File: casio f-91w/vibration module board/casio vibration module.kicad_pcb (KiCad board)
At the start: 2 copper layers, 27 x 25.3 mm, 5 parts

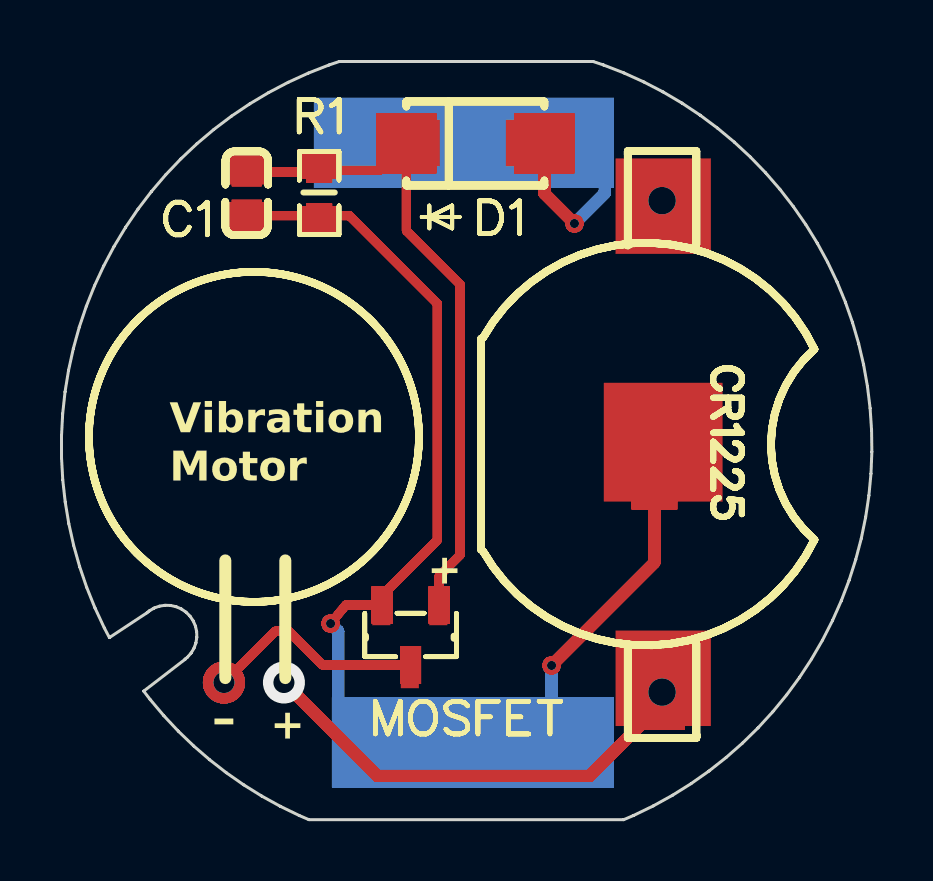
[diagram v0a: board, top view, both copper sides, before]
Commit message: Update vibration module to use 100k resistor
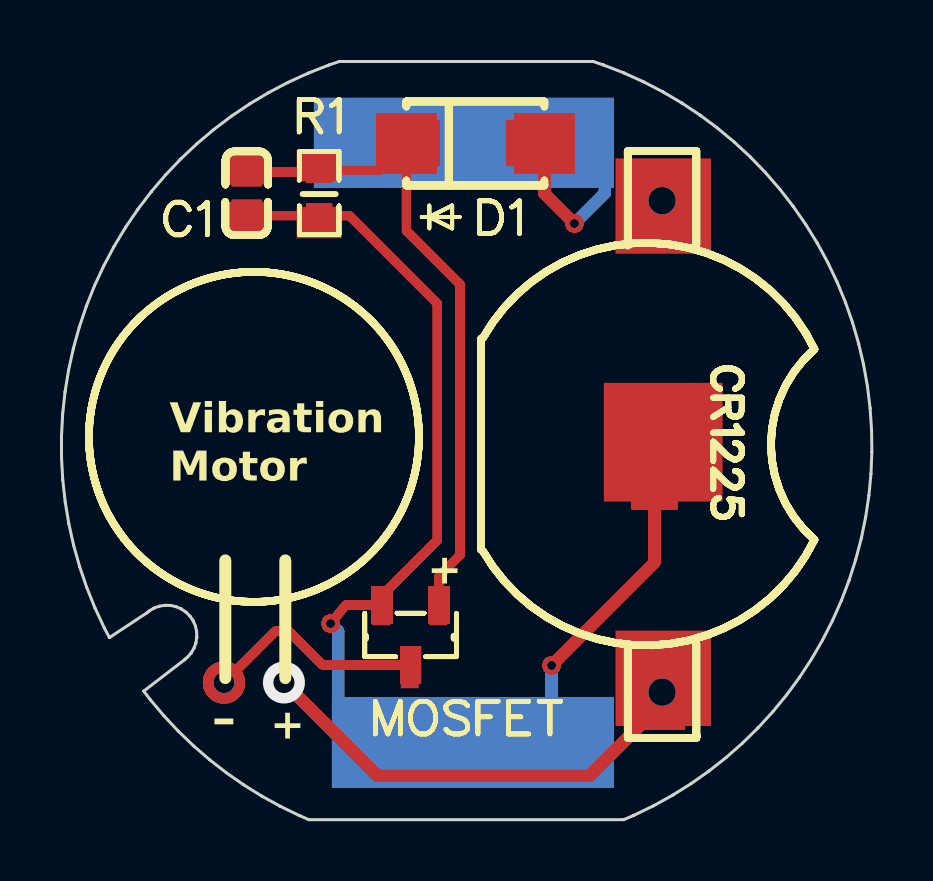
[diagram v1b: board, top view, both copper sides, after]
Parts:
- removed the R** at (135.8, 134.3)
- added R**: RESC2013X65N, footprints:WCR0805LF1003FPLT, F.Cu at (135.8, 134.3)
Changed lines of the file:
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@@
+		)
+	)
+	(footprint "footprints:WCR0805LF1003FPLT"
+		(layer "F.Cu")
+		(at 135.828 134.3276 90)
+		(descr "WCR0805-ren1")
+		(tags "Resistor")
+		(property "Reference" "R**"
+			(at -3.3528 1.7272 -90)
+			(layer "F.SilkS")
+			(hide yes)
+			(effects
+				(font
+					(size 1.27 1.27)
+					(thickness 0.254)
+				)
+			)
+		)
+		(property "Value" "RESC2013X65N"
+			(at -0.05 2.9 -90)
+			(layer "F.SilkS")
+			(hide yes)
+			(effects
+				(font
+					(size 1.27 1.27)
+					(thickness 0.254)
+				)
+			)
+		)
+		(property "Footprint" "footprints:WCR0805LF1003FPLT"
+			(at -0.1 -4.6 90)
+			(unlocked yes)
+			(layer "F.Fab")
+			(hide yes)
+			(effects
+				(font
+					(size 1.27 1.27)
+				)
+			)
+		)
+		(property "Datasheet" ""
+			(at 0 0 90)
+			(unlocked yes)
+			(layer "F.Fab")
+			(hide yes)
+			(effects
+				(font
+					(size 1.27 1.27)
+				)
+			)
+		)
+		(property "Description" ""
+			(at 0 0 90)
+			(unlocked yes)
+			(layer "F.Fab")
+			(hide yes)
+			(effects
+				(font
+					(size 1.27 1.27)
+				)
+			)
+		)
+		(attr smd)
+		(fp_line
+			(start 0 -0.55)
+			(end 0 0.55)
+			(stroke
+				(width 0.2)
+				(type solid)
+			)
+			(layer "F.SilkS")
+		)
+		(fp_line
+			(start 1.725 -1)
+			(end 1.725 1)
+			(stroke
+				(width 0.05)
+				(type solid)
+			)
+			(layer "F.CrtYd")
+		)
+		(fp_line
+			(start -1.725 -1)
+			(end 1.725 -1)
+			(stroke
+				(width 0.05)
+				(type solid)
+			)
+			(layer "F.CrtYd")
+		)
+		(fp_line
+			(start 1.725 1)
+			(end -1.725 1)
+			(stroke
+				(width 0.05)
+				(type solid)
+			)
+			(layer "F.CrtYd")
+		)
+		(fp_line
+			(start -1.725 1)
+			(end -1.725 -1)
+			(stroke
+				(width 0.05)
+				(type solid)
+			)
+			(layer "F.CrtYd")
+		)
+		(fp_line
+			(start 1 -0.65)
+			(end 1 0.65)
+			(stroke
+				(width 0.1)
+				(type solid)
+			)
+			(layer "F.Fab")
+		)
+		(fp_line
+			(start -1 -0.65)
+			(end 1 -0.65)
+			(stroke
+				(width 0.1)
+				(type solid)
+			)
+			(layer "F.Fab")
+		)
+		(fp_line
+			(start 1 0.65)
+			(end -1 0.65)
+			(stroke
+				(width 0.1)
+				(type solid)
+			)
+			(layer "F.Fab")
+		)
+		(fp_line
+			(start -1 0.65)
+			(end -1 -0.65)
+			(stroke
+				(width 0.1)
+				(type solid)
+			)
+			(layer "F.Fab")
+		)
+		(fp_text user "${REFERENCE}"
+			(at 0.2 -3 -90)
+			(layer "F.Fab")
+			(effects
+				(font
+					(size 1.27 1.27)
+					(thickness 0.254)
+				)
+			)
+		)
+		(pad "1" smd rect
+			(at -0.95 0 90)
+			(size 1.05 1.5)
+			(layers "F.Cu" "F.Paste" "F.Mask")
+		)
+		(pad "2" smd rect
+			(at 0.95 0 90)
+			(size 1.05 1.5)
+			(layers "F.Cu" "F.Paste" "F.Mask")
+		)
+		(model "WCR0805LF1003FPLT.stp"
+			(offset
+				(xyz 0 0 0)
+			)
+			(scale
+				(xyz 1 1 1)
+			)
+			(rotate
+				(xyz 0 0 0)
+			)
 		)
 	)
@@
 			)
 		)
-	)
-	(footprint "footprints:RESC2012X60N"
-		(layer "F.Cu")
-		(at 135.825 134.275 90)
-		(descr "CR0805")
-		(tags "Resistor")
-		(property "Reference" "R**"
-			(at 0 0 -90)
-			(layer "F.SilkS")
-			(hide yes)
-			(effects
-				(font
-					(size 1.27 1.27)
-					(thickness 0.254)
-				)
-			)
-		)
-		(property "Value" "RESC2012X60N"
-			(at 0 0 -90)
-			(layer "F.SilkS")
-			(hide yes)
-			(effects
-				(font
-					(size 1.27 1.27)
-					(thickness 0.254)
-				)
-			)
-		)
-		(property "Footprint" "footprints:RESC2012X60N"
-			(at 0 0 90)
-			(unlocked yes)
-			(layer "F.Fab")
-			(hide yes)
-			(effects
-				(font
-					(size 1.27 1.27)
-				)
-			)
-		)
-		(property "Datasheet" ""
-			(at 0 0 90)
-			(unlocked yes)
-			(layer "F.Fab")
-			(hide yes)
-			(effects
-				(font
-					(size 1.27 1.27)
-				)
-			)
-		)
-		(property "Description" ""
-			(at 0 0 90)
-			(unlocked yes)
-			(layer "F.Fab")
-			(hide yes)
-			(effects
-				(font
-					(size 1.27 1.27)
-				)
-			)
-		)
-		(attr smd)
-		(fp_line
-			(start 0 -0.525)
-			(end 0 0.525)
-			(stroke
-				(width 0.2)
-				(type solid)
-			)
-			(layer "F.SilkS")
-		)
-		(fp_line
-			(start 1.7 -1)
-			(end 1.7 1)
-			(stroke
-				(width 0.05)
-				(type solid)
-			)
-			(layer "F.CrtYd")
-		)
-		(fp_line
-			(start -1.7 -1)
-			(end 1.7 -1)
-			(stroke
-				(width 0.05)
-				(type solid)
-			)
-			(layer "F.CrtYd")
-		)
-		(fp_line
-			(start 1.7 1)
-			(end -1.7 1)
-			(stroke
-				(width 0.05)
-				(type solid)
-			)
-			(layer "F.CrtYd")
-		)
-		(fp_line
-			(start -1.7 1)
-			(end -1.7 -1)
-			(stroke
-				(width 0.05)
-				(type solid)
-			)
-			(layer "F.CrtYd")
-		)
-		(fp_line
-			(start 1 -0.625)
-			(end 1 0.625)
-			(stroke
-				(width 0.1)
-				(type solid)
-			)
-			(layer "F.Fab")
-		)
-		(fp_line
-			(start -1 -0.625)
-			(end 1 -0.625)
-			(stroke
-				(width 0.1)
-				(type solid)
-			)
-			(layer "F.Fab")
-		)
-		(fp_line
-			(start 1 0.625)
-			(end -1 0.625)
-			(stroke
-				(width 0.1)
-				(type solid)
-			)
-			(layer "F.Fab")
-		)
-		(fp_line
-			(start -1 0.625)
-			(end -1 -0.625)
-			(stroke
-				(width 0.1)
-				(type solid)
-			)
-			(layer "F.Fab")
-		)
-		(fp_text user "${REFERENCE}"
-			(at 0 0 -90)
-			(layer "F.Fab")
-			(effects
-				(font
-					(size 1.27 1.27)
-					(thickness 0.254)
-				)
-			)
-		)
-		(pad "1" smd rect
-			(at -0.95 0 90)
-			(size 1 1.45)
-			(layers "F.Cu" "F.Paste" "F.Mask")
-		)
-		(pad "2" smd rect
-			(at 0.95 0 90)
-			(size 1 1.45)
-			(layers "F.Cu" "F.Paste" "F.Mask")
-		)
-		(model "CR0805-JW-102ELF.stp"
-			(offset
-				(xyz 0 0 0.2499999962)
-			)
-			(scale
-				(xyz 1 1 1)
-			)
-			(rotate
-				(xyz -90 0 0)
-			)
-		)
